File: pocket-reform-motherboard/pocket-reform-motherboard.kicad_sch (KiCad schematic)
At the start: 313 parts, among them J1 CHARGER, J10 1-2199230-6, J11 Conn_01x33, J12 2199230-5, J13 FH35C-31S-0.3HW(50), J14 USB_C_Receptacle, J15 CONN_SPK, J16 SAMTEC_TSM-106-02-X-SH-A, J17 POWSW, J18 CONN_HEAD, J2 DM3AT-SF-PEJM5, J20 QWIIC, J21 USBSEL, J3 USB_C_Receptacle, J4 09452812561, J5 SYSCTL, J6 USB_INT1, J7 HDMI_D_1.4, J8 SIM_Card, J9 USB_C_Receptacle_USB2.0, SW1 SW_DIP_x01, SW2 RESET, U1 reform2-som-connector, U10 W25Q32JVSS, U11 PCF8523T, U12 AP22815A, U13 TXS0108EPW, U14 SN74AVC1T45, U15 TPD4E02B04DQA, U16 TPD4E02B04DQA, U17 TPD12S521, U18 TLV320AIC3100, U19 TPD4E02B04DQA, U2 MAX1837EUT33+T, U20 TPD4E02B04DQA, U21 TPD4E02B04DQA, U22 TPD4E02B04DQA, U23 FUSB302BMPX, U24 TXS0108EPW, U25 TUSB8041, U26 74HC573, U3 LM2830XQMFE/NOPB, U4 TLV1117-18, U5 TPS5450DDAR, U6 TPS5450DDAR, U7 74LVC1G34, U8 RP2040, U9 TPS7A0533PDBZ, Y1 24MHz, Y2 12MHz 18pF, Y3 32.768 kHz

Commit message: motherboard 1.5: first batch of changes in schematic
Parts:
- removed C16: 330uF, Capacitor_SMD:CP_Elec_6.3x5.4, symbol Device:C_Polarized_Small
- removed C18: 10nF, Capacitor_SMD:C_0603_1608Metric, symbol Device:C_Small
- removed C4, C5: 10uF, Capacitor_SMD:C_0603_1608Metric, symbol Device:C_Small
- removed D11: SS54, Diode_SMD:D_SMA, symbol Device:D_Schottky
- removed D2, D4, D6: PMEG4050EP,115, Diode_SMD:D_SOD-128, symbol Device:D_Schottky_Small_Filled
- removed FB1: 220@100MHz 1.4A, Inductor_SMD:L_0603_1608Metric, symbol Device:FerriteBead_Small
- removed J21: USBSEL, Connector_PinHeader_2.00mm:PinHeader_2x03_P2.00mm_Vertical_SMD, symbol Connector_Generic:Conn_02x03_Odd_Even
- removed J9: USB_C_Receptacle_USB2.0, Connector_USB:USB_C_Receptacle_HRO_TYPE-C-31-M-12, symbol Connector:USB_C_Receptacle_USB2.0
- removed L3, L4: 15uH, Inductor_SMD:L_Vishay_IHLP-4040, symbol Device:L_Small
- removed R17: 10k, Resistor_SMD:R_0402_1005Metric, symbol Device:R_Small
- removed R18: 5.76k, Resistor_SMD:R_0402_1005Metric, symbol Device:R_Small
- removed U12: AP22815A, Package_TO_SOT_SMD:SOT-23-5, symbol reform2:AP22815
- removed U2: MAX1837EUT33+T, Package_TO_SOT_SMD:SOT-23-6, symbol pocket-reform:MAX1837EUT33+T
- removed U5, U6: TPS5450DDAR, Package_SO:TI_SO-PowerPAD-8_ThermalVias, symbol Regulator_Switching:TPS5430DDA
- added C11, C116, C117, C118, C119, C120, C16 (x2), C18: 22uF, Capacitor_SMD:C_0603_1608Metric, symbol Device:C_Polarized_Small
- added C110, C122: 10pF, Capacitor_SMD:C_0402_1005Metric, symbol Device:C_Small
- added C111, C125: 1uF, Capacitor_SMD:C_0402_1005Metric, symbol Device:C_Small
- added C112, C115, C129: 10uF, Capacitor_SMD:C_0603_1608Metric, symbol Device:C_Small
- added C113, C114: 470nF, Capacitor_SMD:C_0603_1608Metric, symbol Device:C_Small
- added C121, C127, C128, C130: 0.1uF, Capacitor_SMD:C_0402_1005Metric, symbol Device:C_Small
- added C4: 1uF, symbol Device:C_Polarized_Small
- added C5: 100uF, symbol Device:C_Polarized_Small
- added D2: ESDS314, Package_TO_SOT_SMD:SOT-23-5, symbol Power_Protection:ESDS304
- added L3: 2.2uH, Inductor_SMD:L_Coilcraft_XAL6060-XXX, symbol Device:L_Small
- added L3: 2.7uH, Inductor_SMD:L_Coilcraft_XAL6060-XXX, symbol Device:L_Small
- added R102: 43.2k, Resistor_SMD:R_0402_1005Metric, symbol Device:R_Small
- added R112, R17, R51, R91: 100k, Resistor_SMD:R_0402_1005Metric, symbol Device:R_Small
- added R113, R114, R115, R116, R117, R118, R119, R121, R17, R49, R94: 10k, Resistor_SMD:R_0402_1005Metric, symbol Device:R_Small
- added R120: 4.7k, symbol Device:R_Small
- added R18, R92: 4.99k, Resistor_SMD:R_0402_1005Metric, symbol Device:R_Small
- added R18: 24.9k, Resistor_SMD:R_0402_1005Metric, symbol Device:R_Small
- added R31: 0, Resistor_SMD:R_0603_1608Metric, symbol Device:R_Small
- added R32: 6.8k, symbol Device:R_Small
- added R63, R71: 1k, Resistor_SMD:R_0402_1005Metric, symbol Device:R_Small
- added U12, U32: AP22615AWU-7, Package_TO_SOT_SMD:SOT-23-6, symbol Regulator_Linear:AP22615AWU
- added U2, U30, U31: TS3USB30EDGSR, Package_SO:VSSOP-10_3x3mm_P0.5mm, symbol Interface_USB:TS3USB30EDGSR
- added U27: TVS2200DRV, Package_SON:WSON-6-1EP_2x2mm_P0.65mm_EP1x1.6mm, symbol Power_Protection:TVS2200DRV
- added U28, U6: LM62460, footprints:CONV_LM61495QRPHRQ1, symbol LM62460:LM62460
- added U29: TPS62177DQC, Package_SON:WSON-10-1EP_2x3mm_P0.5mm_EP0.84x2.4mm_ThermalVias, symbol Regulator_Switching:TPS62177DQC
- added U33: AT24CS02-STUM, Package_TO_SOT_SMD:SOT-23-5, symbol Memory_EEPROM:AT24CS02-STUM
- added U5: LM73100RPWR, LM73100RPWR:IC_LM73100RPWR, symbol LM73100RPWR:LM73100RPWR
- C11, C8: value 10nF -> 470nF; Manufacturer_No CL10B103KB8NNNC -> CL10A474KB8NNNC
- C12, C7: value 10nF -> 10uF; LCSC C1589 -> C92487; Manufacturer_No CL10B103KB8NNNC -> GRM188R61E106KA73J
- C15: value 330uF -> 22uF; footprint Capacitor_SMD:CP_Elec_6.3x5.4 -> Capacitor_SMD:C_0603_1608Metric; LCSC C286137 -> C140782; Manufacturer Lelon -> Murata; Manufacturer_No VZT331M0JTR-0606ACS -> GRM187R61A226ME15D
- C19: value 10nF -> 0.1uF; footprint Capacitor_SMD:C_0603_1608Metric -> Capacitor_SMD:C_0402_1005Metric; Manufacturer_No CL10B103KB8NNNC -> CL05B104KO5NNNC
- L1: value 22uH -> 10uH; footprint Inductor_SMD:L_Taiyo-Yuden_NR-30xx -> (none); LCSC C92953 -> (none); Manufacturer YJYCOIN -> (none); Manufacturer_No YNR3015-150M -> (none)
- R15: value 10k -> 47k; footprint Resistor_SMD:R_0402_1005Metric -> (none); LCSC C60490 -> (none); Manufacturer Yageo -> (none); Manufacturer_No RC0402FR-0710KL -> (none)
- R16: value 3.16k -> 1k; footprint Resistor_SMD:R_0402_1005Metric -> (none); LCSC C163466 -> (none); Manufacturer Yageo -> (none); Manufacturer_No RC0402FR-073K16L -> (none)
- R55, R86: Manufacturer DNP -> Yageo; Manufacturer_No DNP -> RC0402FR-0733RL
- R6: value 100k -> 470k; footprint Resistor_SMD:R_0402_1005Metric -> (none); LCSC C60491 -> (none); Manufacturer Yageo -> (none); Manufacturer_No RC0402FR-07100KL -> (none)
- R62: value DNP -> 0; LCSC DNP -> C242160; Manufacturer DNP -> Panasonic; Manufacturer_No DNP -> ERJ2GE0R00X
- R7: value 100k -> 11k; footprint Resistor_SMD:R_0402_1005Metric -> (none); LCSC C60491 -> (none); Manufacturer Yageo -> (none); Manufacturer_No RC0402FR-07100KL -> (none)
- R9: value 0 -> 100k; LCSC C242160 -> C60490; Manufacturer Panasonic -> Yageo; Manufacturer_No ERJ2GE0R00X -> RC0402FR-07100KL
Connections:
- net +3V3: now also C116.1, C117.1, C118.1, C119.1, C120.1, L3.2, R112.2, R91.1, R92.1, U28.5 (BIAS); no longer C19.2
- net +5V: now also C39.1, R62.1, C11.1, C16.1, C16.1, C18.1, L3.2, R17.1, R18.1, R51.2, U12.6 (IN), U6.5 (BIAS); no longer J3.A4 (VBUS), J3.A9 (VBUS), J3.B4 (VBUS), J3.B9 (VBUS), R15.1, R62.2, R83.2, R84.2
- net GND: now also C11.2, C12.2, R15.2, C11.2, C111.1, C112.2, C113.2, C114.2, C115.2, C116.2, C117.2, C118.2, C119.2, C120.2, C125.1, C129.2, C130.2, C16.2, C16.2, C18.2, C4.2, C5.2, D2.2 (A), R102.2, R115.2, R116.2, R118.2, R120.2, R121.1, R17.2, R18.2, R32.2, R49.1, R94.2, U12.2 (GND), U2.5 (GND), U27.1 (GND), U27.2 (GND), U27.3 (GND), U27.7 (GND), U28.1 (PGND2), U28.12 (SYNC/MODE), U28.15 (PGND1), U28.8 (AGND), U29.1 (PGND), U29.11 (PAD), U29.5 (FB), U29.6 (AGND), U30.5 (GND), U31.5 (GND), U32.2 (GND), U33.2 (GND), U33.5 (WP), U5.8 (GND), U6.1 (PGND2), U6.12 (SYNC/MODE), U6.15 (PGND1), U6.8 (AGND); no longer C19.1, D5.2 (A), R6.2, R7.2, R9.2
- net RP_SCL0: now also D2.4 (K), U33.1 (SCL)
- net RP_SDA0: now also D2.3 (K), U33.3 (SDA)
- net RUD+: now also U2.3 (D2+), U30.4 (D+)
- net RUD-: now also U2.7 (D2-), U30.6 (D-)
- net STANDBY_3V3: now also R9.2, C130.1, R113.1, R114.1, R117.1, U2.10 (VCC), U29.10 (VOS), U30.10 (VCC), U31.10 (VCC), U33.4 (VCC)
- net USB1_RXN: now also C128.1; no longer U25.56 (USB_SSTXM_UP)
- net USB1_RXP: now also C127.1; no longer U25.55 (USB_SSTXP_UP)
- net USB2_DN: now also U2.8 (D1-), U30.8 (D1-)
- net USB2_DP: now also U2.2 (D1+), U30.2 (D1+)
- net USBH_1_DN: now also U31.8 (D1-); no longer J3.A7 (D-), J3.B7 (D-), U16.4 (IO3), U16.7 (IO3)
- net USBH_1_DP: now also U31.2 (D1+); no longer J3.A6 (D+), J3.B6 (D+), U16.5 (IO4), U16.6 (IO4)
- net USB_SRC_EN: now also R49.2, U12.4 (EN)
- net USB_VBUS: now also R31.2, U27.4 (IN), U27.5 (IN), U27.6 (IN)
- net VCC: now also C11.1, C12.1, D5.1 (K), C129.1, C5.1, R119.2, U29.2 (VIN), U32.6 (IN), U5.6 (OUT), U6.14 (VIN1), U6.2 (VIN2); no longer J1.1 (Pin_1), J1.2 (Pin_2)
- net VCHG: now also D5.2 (A), R31.1
- net XUD+: now also U2.4 (D+), U31.3 (D2+)
- net XUD-: now also U2.6 (D-), U31.7 (D2-)
- net ~{STANDBY_SHDN}: now also U29.3 (EN)
- net at J6.1 (Pin_1): now also R62.2; no longer C39.1
- net at R16.1: now also U5.9 (IMON); no longer R15.2
- net at R6.1: now also J1.1 (Pin_1), J1.2 (Pin_2), C4.1, U5.5 (IN); no longer U26.19 (Q0)
- net at U26.18 (Q1): now also R71.2; no longer R7.1
- net at R68.1: now also U12.3 (FLG)
- net at R9.1: now also U29.7 (PG)
- net at L1.1: now also U29.9 (SW)
- new net: R113.2, U30.1 (S)
- new net: C111.2, U6.11 (SPSP), U6.6 (VCC), U6.9 (RT)
- new net: R119.1, U32.3 (FLG)
- new net: R63.2, U26.19 (Q0)
- new net: R114.2, U2.1 (S)
- new net: R51.1, U6.10 (RESET)
- new net: C19.2, L3.1, U6.16 (SW)
- new net: C19.1, U6.3 (RBOOT), U6.4 (CBOOT)
- new net: C110.1, R17.2, R18.1, U6.7 (FB)
- new net: C122.1, R102.1, R91.2, U28.7 (FB)
- new net: C122.2, R92.2
- new net: R120.1, U32.5 (ISET)
- new net: R112.1, U28.10 (RESET)
- new net: R15.1, R7.2, U5.2 (OVLO)
- new net: C121.2, L3.1, U28.16 (SW)
- new net: R115.1, U2.9 (~{OE})
- new net: R6.2, R7.1, U5.1 (EN/UVLO)
- new net: C110.2, R18.2
- new net: R117.2, U31.1 (S)
- new net: R32.1, U12.5 (ISET)
- new net: C125.2, U28.11 (SPSP), U28.6 (VCC), U28.9 (RT)
- new net: C121.1, U28.3 (RBOOT), U28.4 (CBOOT)
- new net: R116.1, U30.9 (~{OE})
- new net: R118.1, U31.9 (~{OE})
- new net 3V3_ENABLE_L: R121.2, R71.1, R94.1, U28.13 (EN), U32.4 (EN)
- new net 5V_ENABLE_L: R17.1, R63.1, U6.13 (EN)
- new net USB1_C_RXN: C128.2, U25.56 (USB_SSTXM_UP)
- new net USB1_C_RXP: C127.2, U25.55 (USB_SSTXP_UP)
- new net USB_P2_DN: J3.A7 (D-), J3.B7 (D-), U16.4 (IO3), U16.7 (IO3), U31.6 (D-)
- new net USB_P2_DP: J3.A6 (D+), J3.B6 (D+), U16.5 (IO4), U16.6 (IO4), U31.4 (D+)
- new net USB_VBUS2: J3.A4 (VBUS), J3.A9 (VBUS), J3.B4 (VBUS), J3.B9 (VBUS), R83.2, R84.2, U12.1 (OUT)
- new net VIN_FOR_3V3: C112.1, C113.1, C114.1, C115.1, U28.14 (VIN1), U28.2 (VIN2), U32.1 (OUT)
- no-connect marks 198 -> 200
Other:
- note added: "22k = 1.5A @ 5V limit"
- note added: "4.75-28V"
- note added: "500mA"
- note added: "62177 has fixed 3.3V out"
- note added: "Cff"
- note added: "Charger: MP2650"
- note added: "External port 2 USB 2.0"
- note added: "ILIM (A) = 6800/RLIM (Ω)"
- note added: "ILIM (A) = 6800/RLIM (Ω) = ~1.45A"
- note added: "MAX 28V"
- note added: "Rfbb"
- note added: "Rfbt"
- note added: "Rff"
- note added: "S=0: D=D1 S=1: D=D2"
- note added: "SOC USB recovery port"
- note added: "TODO: 10uF input cap!"
- note added: "TODO: 10uF/47uF output cap!"
- note added: "TODO: S/OE matrix"
- note added: "TODO: S_3V3 caps"
- note added: "TODO: any current limiting / monitoring here?"
- note added: "TODO: bulk cap"
- note added: "TODO: calc. all resistor values"
- note added: "TODO: clean up choke values mess"
- note added: "TODO: compare crystal to reference"
- note added: "TODO: confirm address (conflicts?)"
- note added: "TODO: double check for RK3588"
- note added: "TODO: fix 1uF locations!"
- note added: "TODO: limit"
- note added: "TODO: missing AC caps on TX lines"
- note added: "TODO: move status LED to this port"
- note added: "TODO: replace with i2c solution from next?"
- note added: "TODO: serial to SBU?"
- note added: "TODO: sleep pin"
- note added: "TODO: test points for I2C+STANDBY_3V3"
- note added: "TODO: test points for all power rails"
- note added: "TSOT-23-6"
- note added: "To charger (SINK/SOURCE)"
- note added: "automatic charger board bypass"
- note added: "default"
- note added: "default must be for flashing the rp2040 from the outside. rp2040 can then switch this to other functions."
- note added: "ideal diode ->"
- note added: "place near RP2040"
- note added: "there was a diode here in V1.0 pointing towards VCHG. since V1.5, VCHG can also output to the USB-C port (use OTG VBUS function)."
- note removed: "250mA"
- note removed: "4.5-24V"
- note removed: "5A"
- note removed: "=3.34V"
- note removed: "=5.085V"
- note removed: "Charger: MP2762A"
- note removed: "MAX 24V"
- note removed: "NRH3012T220MN"
- note removed: "ROQANG RVT0J331M0605"
- note removed: "This pair of jumpers connects RP2040 (SYSCON) to either the SOC or the J9 USB port."
- note removed: "To charger (SINK)"
- note removed: "input shutdown current: 7uA (3uA?)"
- moved on the sheet: C1, C10, C100, C101, C14, C2, C21, C23, C3, C38, C39, C47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

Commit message: pref mainboard 1.5: schematic/routing progress
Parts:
- removed C11, C16 (x2): 22uF, Capacitor_SMD:C_0603_1608Metric, symbol Device:C_Polarized_Small
- removed C17: 22uF, Capacitor_SMD:C_0603_1608Metric, symbol Device:C_Small
- removed L3: 2.2uH, Inductor_SMD:L_Coilcraft_XAL6060-XXX, symbol Device:L_Small
- removed R17: 10k, Resistor_SMD:R_0402_1005Metric, symbol Device:R_Small
- removed R18: 4.99k, Resistor_SMD:R_0402_1005Metric, symbol Device:R_Small
- removed TP5, TP6: TestPoint, TestPoint:TestPoint_Pad_D1.0mm, symbol Connector:TestPoint
- added C131: 0.1uF, Capacitor_SMD:C_0402_1005Metric, symbol Device:C_Small
- added C134: 22uF, Capacitor_SMD:C_0603_1608Metric, symbol Device:C_Small
- added C135: 47uF, Capacitor_SMD:C_1206_3216Metric, symbol Device:C_Polarized_Small
- added C16, C17: 22uF, Capacitor_SMD:C_0603_1608Metric, symbol Device:C_Polarized_Small
- added J61: UART, Connector_JST:JST_SH_SM04B-SRSS-TB_1x04-1MP_P1.00mm_Horizontal, symbol Connector_Generic:Conn_01x04
- added L4: 2.2uH, Inductor_SMD:L_Coilcraft_XAL6060-XXX, symbol Device:L_Small
- added R122, R123, R124: 0, Resistor_SMD:R_0402_1005Metric, symbol Device:R_Small
- added R125: 10k, Resistor_SMD:R_0402_1005Metric, symbol Device:R_Small
- added R126: 4.99k, Resistor_SMD:R_0402_1005Metric, symbol Device:R_Small
- added U34: PCA9536DP, Package_SO:TSSOP-8_3x3mm_P0.65mm, symbol Interface_Expansion:PCA9536DP
- C14: value 47uF -> 22uF; Manufacturer_No GRM188R60J476ME15D -> GRM187R61A226ME15D
- C22, C24: value 27pF -> 15pF; LCSC C107045 -> C161530; Manufacturer Yageo -> Murata; Manufacturer_No CC0603JRNPO9BN270 -> GRM1555C1H150FA01D
- C4: footprint (none) -> Capacitor_SMD:C_0603_1608Metric
- C5: value 100uF -> 47uF; footprint (none) -> Capacitor_SMD:CP_Elec_6.3x5.8
- C83: footprint Capacitor_SMD:C_0603_1608Metric -> Capacitor_SMD:C_1206_3216Metric
- J7: footprint Connector_HDMI:HDMI_Micro-D_Molex_46765-0x01 -> Connector_Video:HDMI_Micro-D_Molex_46765-0x01
- L1: footprint (none) -> Inductor_SMD:L_1210_3225Metric
- R116, R118: value 10k -> 0; Manufacturer Yageo -> Panasonic; Manufacturer_No RC0402JR-0710KL -> ERJ2GE0R00X
- R120, R15, R16, R32, R6, R7: footprint (none) -> Resistor_SMD:R_0402_1005Metric
- U10: footprint Package_SO:SOIC-8_5.23x5.23mm_P1.27mm -> Package_SO:SOIC-8_5.3x5.3mm_P1.27mm
- U5: footprint LM73100RPWR:IC_LM73100RPWR -> footprints:IC_LM73100RPWR
- Y2: value 12MHz 18pF -> 12MHz 12pF; LCSC C91749 -> C20625731; Manufacturer Seiko Epson -> Abracon; Manufacturer_No Q22FA23V0041800 -> ABM8-272-T3
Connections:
- net +1V1: now also C134.1
- net +3V3: now also J61.1 (Pin_1), L4.2
- net +5V: now also C14.1, C16.1, C17.1, R126.1
- net 3V3_ENABLE_L: now also R71.2, U26.18 (Q1); no longer R71.1, R94.1, U28.13 (EN)
- net 5V_ENABLE_L: now also R63.2, U26.19 (Q0); no longer R63.1, U6.13 (EN)
- net GND: now also C131.2, C134.2, C135.2, C16.2, C17.2, J61.3 (Pin_3), R125.2, U34.4 (VSS); no longer R116.2, R118.2
- net STANDBY_3V3: now also R117.2, C131.1, C135.1, U34.8 (VDD); no longer C14.1, C29.1, R117.1
- net SWC: now also J61.2 (Pin_2)
- net SWD: now also J61.4 (Pin_4)
- net at U1.139 (FAST_BOOT): now also R116.1
- net CHG_VCC: now reaches C4.1, J1.1 (Pin_1), J1.2 (Pin_2), R6.1, U5.5 (IN)
- net USWITCH_3: now reaches R113.2, U30.1 (S)
- net USWITCH_3: now also R124.2
- net USWITCH_2: now reaches R114.2, U2.1 (S)
- net USWITCH_2: now also R123.2
- net at C26.1, C28.1, C30.1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: now also C29.1
- net USB_LOADER_SW: now reaches U8.38 (GPIO26_ADC0)
- net USB_LOADER_SW: now also R116.2
- net 1V1_ENABLE_L: now reaches R8.1, U26.17 (Q2), U3.4 (EN)
- net at C121.2, U28.16 (SW): now also L4.1
- net at R115.1: now also R118.1, U34.5 (IO3); no longer U2.9 (~{OE})
- net at C110.2: now also R126.2
- net USWITCH_1: now reaches U31.1 (S)
- net USWITCH_1: now also R117.1, R122.2; no longer R117.2
- net USWITCH_OFF: now reaches U30.9 (~{OE})
- net USWITCH_OFF: now also R118.2, U2.9 (~{OE}), U31.9 (~{OE}); no longer R116.1
- new net: R125.1, R63.1, U6.13 (EN)
- new net: R122.1, U34.1 (IO0)
- new net: R123.1, U34.2 (IO1)
- new net: R124.1, U34.3 (IO2)
- new net: R71.1, R94.1, U28.13 (EN)
- new net RP_SCL1: U34.6 (SCL)
- new net RP_SDA1: U34.7 (SDA)
- no-connect marks 200 -> 196
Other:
- note added: "- Display V1: Backlight is digitally controlled - Display V2: Backlight is PWMed by RP2040 on DISP_EN_L pin"
- note added: "New in V1.5"
- note added: "SOC USB recovery port - UUU on i.MX8MP - EDL on QUASAR - BootRom/xrock on RK3588"
- note added: "SWD Debug"
- note added: "Switch for 2nd USB routing"
- note added: "TODO: C4 cap size"
- note added: "TODO: sleep pin ??"
- note added: "close to VREG_IN"
- note added: "close to VREG_OUT"
- note added: "display enable on V2?"
- note removed: "Backlight is digitally controlled"
- note removed: "SOC USB recovery port"
- note removed: "TODO: double check for RK3588"
- note removed: "TODO: sleep pin"
- moved on the sheet: C15, C26, C28, C29, C30, R113, R114, R115, R117, U2, U30, U31

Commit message: pref mainboard v1.5 place+route progress
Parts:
- removed R103, R111: 0, Resistor_SMD:R_0402_1005Metric, symbol Device:R_Small
- C21, C23: footprint Capacitor_SMD:C_0603_1608Metric -> Capacitor_SMD:C_0402_1005Metric; LCSC C107040 -> (none); Manufacturer_No CC0603JRNPO9BN180 -> (none)
- C83: footprint Capacitor_SMD:C_1206_3216Metric -> Capacitor_SMD:C_0603_1608Metric
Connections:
- net RP_SCL1 is gone; now on net RP_SCL0: U34.6 (SCL)
- net RP_SDA1 is gone; now on net RP_SDA0: U34.7 (SDA)
- net USBH_1B_AC_TXN: now also U22.1 (IO1), U22.10 (IO1); no longer U22.4 (IO3), U22.7 (IO3)
- net USBH_1B_AC_TXP: now also U22.2 (IO2), U22.9 (IO2); no longer U22.5 (IO4), U22.6 (IO4)
- net USBH_1B_RXN: now also U22.4 (IO3), U22.7 (IO3); no longer U22.1 (IO1), U22.10 (IO1)
- net USBH_1B_RXP: now also U22.5 (IO4), U22.6 (IO4); no longer U22.2 (IO2), U22.9 (IO2)
- net at J14.A5 (CC1), U15.1 (IO1), U15.10 (IO1): now also U23.10 (CC1), U23.11 (CC1)
- net at J14.B5 (CC2), U15.2 (IO2), U15.9 (IO2): now also U23.1 (CC2), U23.14 (CC2)

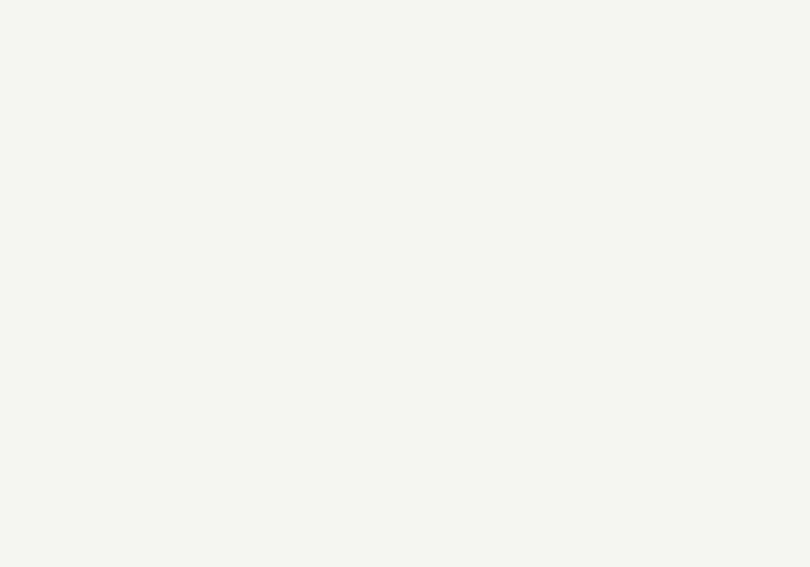
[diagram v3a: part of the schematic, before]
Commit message: pref mainboard v1.5 place+route progress
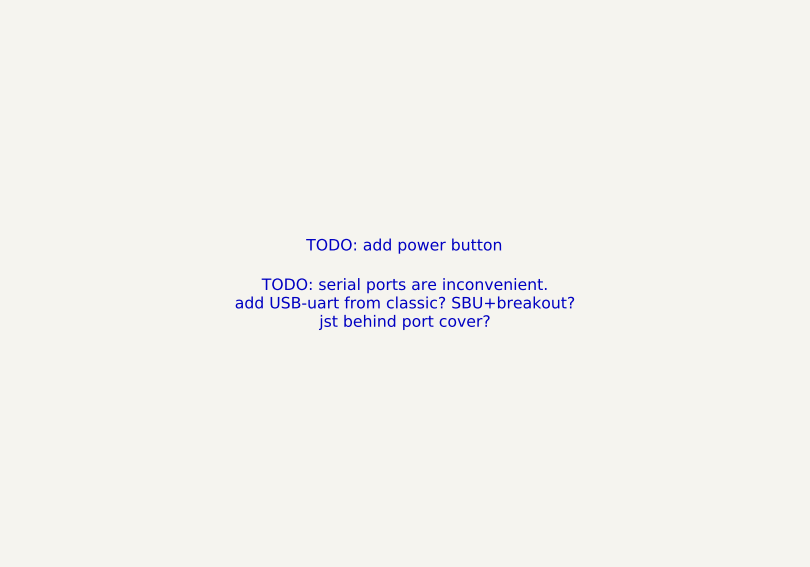
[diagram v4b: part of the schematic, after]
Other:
- note added: "TODO: add power button"
- note added: "TODO: serial ports are inconvenient. add USB-uart from classic? SBU+breakout? jst behind port cover?"
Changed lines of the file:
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@@
+		)
+	)
+	(text "TODO: add power button"
+		(exclude_from_sim no)
+		(at 584.1253 101.514 0)
+		(effects
+			(font
+				(size 1.27 1.27)
+			)
 		)
 	)
@@
 		)
 	)
+	(text "TODO: serial ports are inconvenient.\nadd USB-uart from classic? SBU+breakout?\njst behind port cover?"
+		(exclude_from_sim no)
+		(at 584.2 107.95 0)
+		(effects
+			(font
+				(size 1.27 1.27)
+			)
+		)
+	)

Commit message: mb1.5: displayport alt mode schematic WIP
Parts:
- added C132, C133, C136: 0.1uF, Capacitor_SMD:C_0402_1005Metric, symbol Device:C_Small
- added C137, C138, C139, C140: 0.22uF, Capacitor_SMD:C_0402_1005Metric, symbol Device:C_Small
- added J9: Conn_01x20, Connector_FFC-FPC:Hirose_FH12-20S-0.5SH_1x20-1MP_P0.50mm_Horizontal, symbol Connector_Generic:Conn_01x20
- added R103: 0, Resistor_SMD:R_0402_1005Metric, symbol Device:R_Small
- added R111, R127: 10k, Resistor_SMD:R_0402_1005Metric, symbol Device:R_Small
- added R150, R157: 100k, Resistor_SMD:R_0402_1005Metric, symbol Device:R_Small
- added U35: TMUXHS4446RETR, TMUXHS4446RETR:IC_TMUXHS4446RETR, symbol TMUXHS4446RETR:TMUXHS4446RETR
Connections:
- net STANDBY_3V3 is gone; now on net VCC: C109.1, C13.2, C130.1, C131.1, C135.1, C25.1, C27.1, C31.1, C32.1, C33.1, C34.1, C35.1, C36.1, C40.1, C46.2, J1.5 (Pin_5), J20.2 (Pin_2), J5.1 (Pin_1), L1.2, R113.1, R114.1, R117.2, R19.2, R38.1, R56.1, R57.2, R59.2, R9.2, U10.8 (VCC), U11.8 (VDD), U2.10 (VCC), U23.3 (VDD), U23.4 (VDD), U26.20 (VCC), U29.10 (VOS), U30.10 (VCC), U31.10 (VCC), U33.4 (VCC), U34.8 (VDD), U8.1 (IOVDD), U8.10 (IOVDD), U8.22 (IOVDD), U8.33 (IOVDD), U8.42 (IOVDD), U8.43 (ADC_AVDD), U8.44 (VREG_IN), U8.48 (USB_VDD), U8.49 (IOVDD)
- net +3V3: now also R157.1
- net +5V: now also R103.2
- net GND: now also C132.1, J9.12 (Pin_12), J9.13 (Pin_13), J9.3 (Pin_3), J9.6 (Pin_6), J9.9 (Pin_9), R150.2, U35.15 (GND), U35.18 (GND), U35.37 (GND), U35.41 (GND)
- net RP_SCL0: now also U35.36 (CONF1/SCL)
- net RP_SDA0: now also U35.38 (CONF2/SDA)
- net USBH_2A_RXN: now also U35.17 (SSRX-); no longer J14.B10 (RX1-), U19.1 (IO1), U19.10 (IO1)
- net USBH_2A_RXP: now also U35.16 (SSRX+); no longer J14.B11 (RX1+), U19.2 (IO2), U19.9 (IO2)
- net USBH_2A_TXN: now also U35.12 (SSTX-); no longer C90.2
- net USBH_2A_TXP: now also U35.11 (SSTX+); no longer C92.2
- net USBH_2B_AC_TXN: no longer C91.1, J14.B3 (TX2-), U21.4 (IO3), U21.7 (IO3)
- net USBH_2B_AC_TXP: no longer C93.1, J14.B2 (TX2+), U21.5 (IO4), U21.6 (IO4)
- net USBH_2B_RXN: no longer J14.A10 (RX2-), U21.1 (IO1), U21.10 (IO1)
- net USBH_2B_RXP: no longer J14.A11 (RX2+), U21.2 (IO2), U21.9 (IO2)
- net USBH_2B_TXN: no longer C91.2
- net USBH_2B_TXP: no longer C93.2
- net VCC: now also C132.2, R111.2, R127.2, U35.10 (VCC), U35.23 (VCC), U35.26 (VCC), U35.29 (VCC), U35.32 (VCC), U35.4 (VCC), U35.7 (VCC)
- net USBH_2A_AC_TXN renamed USBM1_AC_TXN
- net USBM1_AC_TXN: now also C92.2; no longer C90.1
- net USBH_2A_AC_TXP renamed USBM1_AC_TXP
- net USBM1_AC_TXP: now also C90.2; no longer C92.1
- new net: J9.18 (Pin_18), J9.19 (Pin_19), J9.20 (Pin_20), R103.1
- new net: R111.1, U35.1 (MODE0)
- new net: R127.1, U35.13 (MODE1)
- new net: C92.1, U35.27 (CTX1-)
- new net: C90.1, U35.28 (CTX1+)
- new net: C93.1, U35.30 (CTX2-)
- new net: C91.1, U35.31 (CTX2+)
- new net DP0_N: C137.1, J9.8 (Pin_8)
- new net DP0_P: C138.1, J9.7 (Pin_7)
- new net DP1_N: C139.1, J9.5 (Pin_5)
- new net DP1_P: C140.1, J9.4 (Pin_4)
- new net DP_AUX_N: C136.1, J9.15 (Pin_15)
- new net DP_AUX_P: C133.1, J9.16 (Pin_16)
- new net DP_HPD: J9.17 (Pin_17)
- new net USBM1_AC_RXN: J14.B10 (RX1-), U19.1 (IO1), U19.10 (IO1), U35.24 (CRX1-)
- new net USBM1_AC_RXP: J14.B11 (RX1+), U19.2 (IO2), U19.9 (IO2), U35.25 (CRX1+)
- new net USBM2_AC_RXN: J14.A10 (RX2-), U21.1 (IO1), U21.10 (IO1), U35.33 (CRX2-)
- new net USBM2_AC_RXP: J14.A11 (RX2+), U21.2 (IO2), U21.9 (IO2), U35.34 (CRX2+)
- new net USBM2_AC_TXN: C93.2, J14.B3 (TX2-), U21.4 (IO3), U21.7 (IO3)
- new net USBM2_AC_TXP: C91.2, J14.B2 (TX2+), U21.5 (IO4), U21.6 (IO4)
- new net USBM_DP0_N: C137.2, U35.40 (DP0-)
- new net USBM_DP0_P: C138.2, U35.39 (DP0+)
- new net USBM_DP1_N: C139.2, U35.3 (DP1-)
- new net USBM_DP1_P: C140.2, U35.2 (DP1+)
- new net USBM_DP_AUX_N: C136.2, R157.2, U35.20 (AUX-)
- new net USBM_DP_AUX_P: C133.2, R150.1, U35.19 (AUX+)
- new net USBM_SBU1: U35.22 (SBU1)
- new net USBM_SBU2: U35.21 (SBU2)
- no-connect marks 196 -> 205
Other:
- note added: "3v3 I2C Mode"
- note added: "DP from SOM TODO: flip?!"
- note added: "DisplayPort"
- note added: "DisplayPort Alt-Mode Mux"
- note added: "TODO: HPD to SYSCTL?"
- note added: "TODO: address bits"
- note added: "TODO: any termination needed?"
- note added: "TODO: can we bypass latch for disp v2 pwm?"
- note added: "TODO: leftover"
- note added: "TODO: missing AC caps here to host? double check"
- note added: "TODO: missing AC caps on TX lines? double check"
- note added: "TODO: serial 2 here?"
- note removed: "TODO: missing AC caps on TX lines"
- note removed: "consider: ANX7580 eDP -> DSI to integrate LS1028A"
- moved on the sheet: C90, C91, C92, C93
